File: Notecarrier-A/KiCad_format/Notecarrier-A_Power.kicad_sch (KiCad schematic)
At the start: 42 parts, among them J10 00711, J12 B2B-PH-SM4-TBT(LF)(SN), J19 MICROUSB-B, J2 B2B-PH-SM4-TBT(LF)(SN), J4 B2B-PH-SM4-TBT(LF)(SN), J9 12734, SW1 CJS-1200TA, U2 BQ24210DQCT, U3 MAX17225ELT, U4 TPS62748YFPT

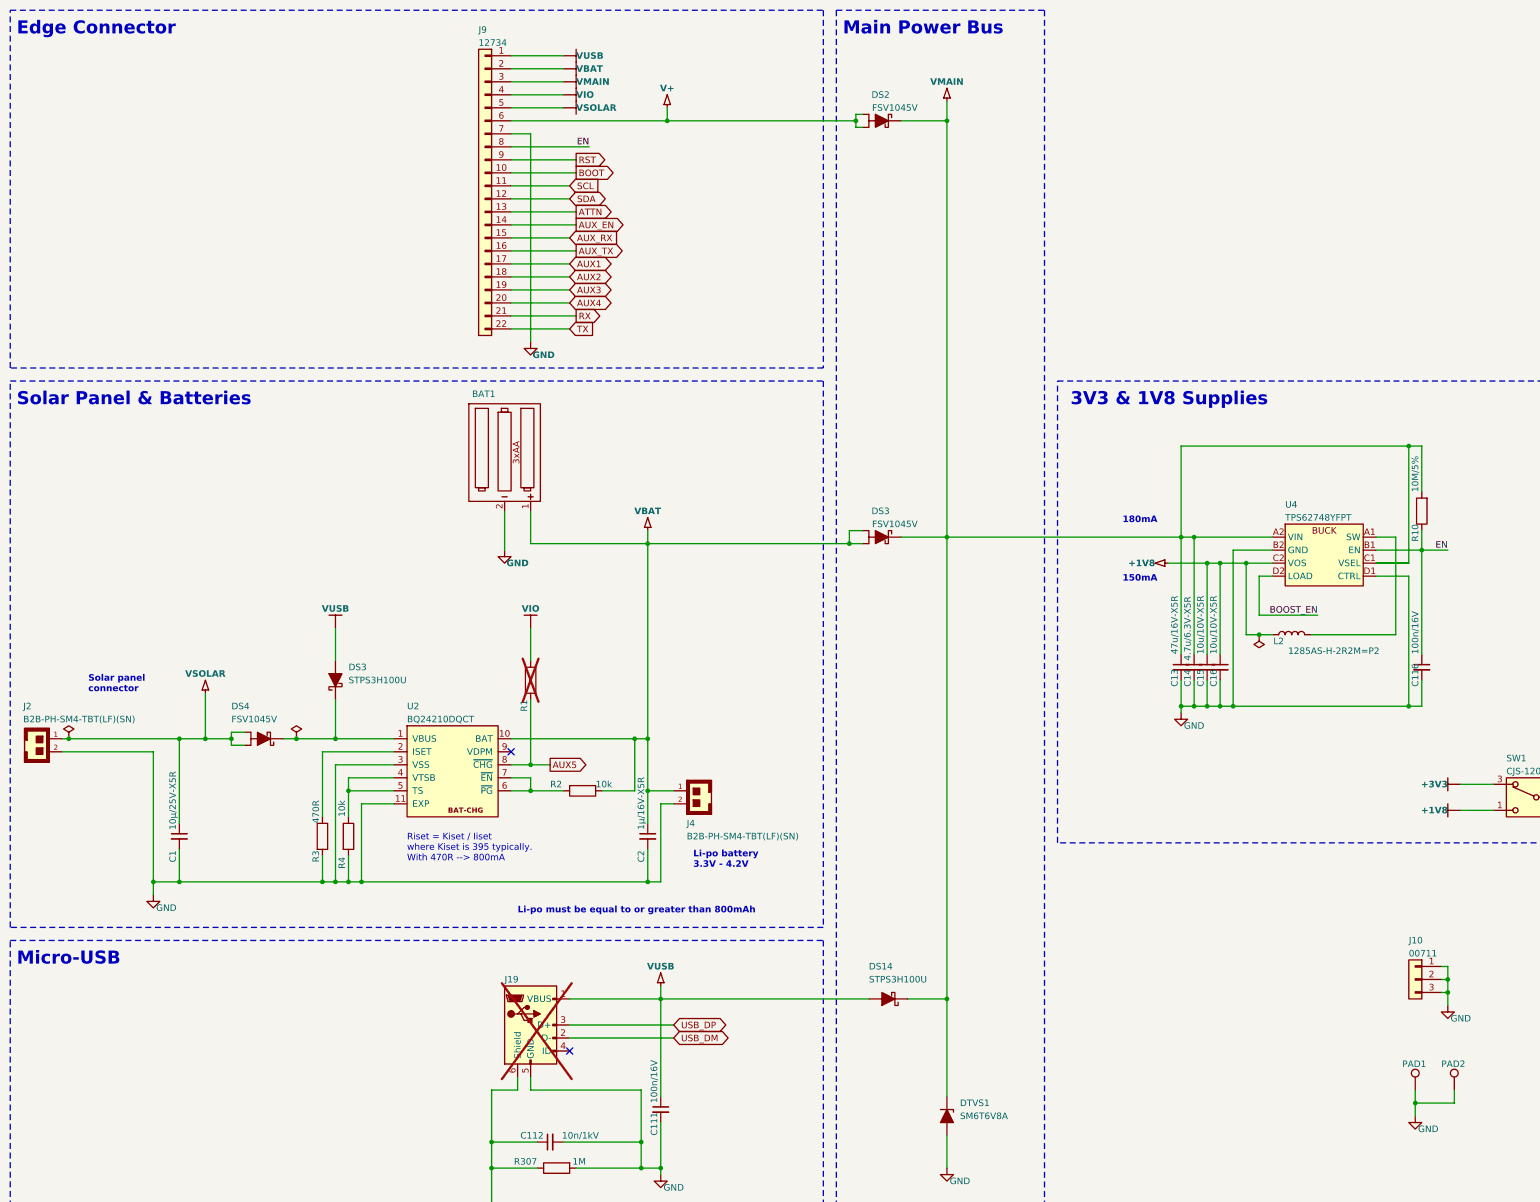
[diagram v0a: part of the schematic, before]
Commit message: Establish port of Notecarrier-B PCB.
Ported: components, board outline, fabrication layers, silkscreens and front copper.
To go: inner and back copper layers, drills, sheet metadata.
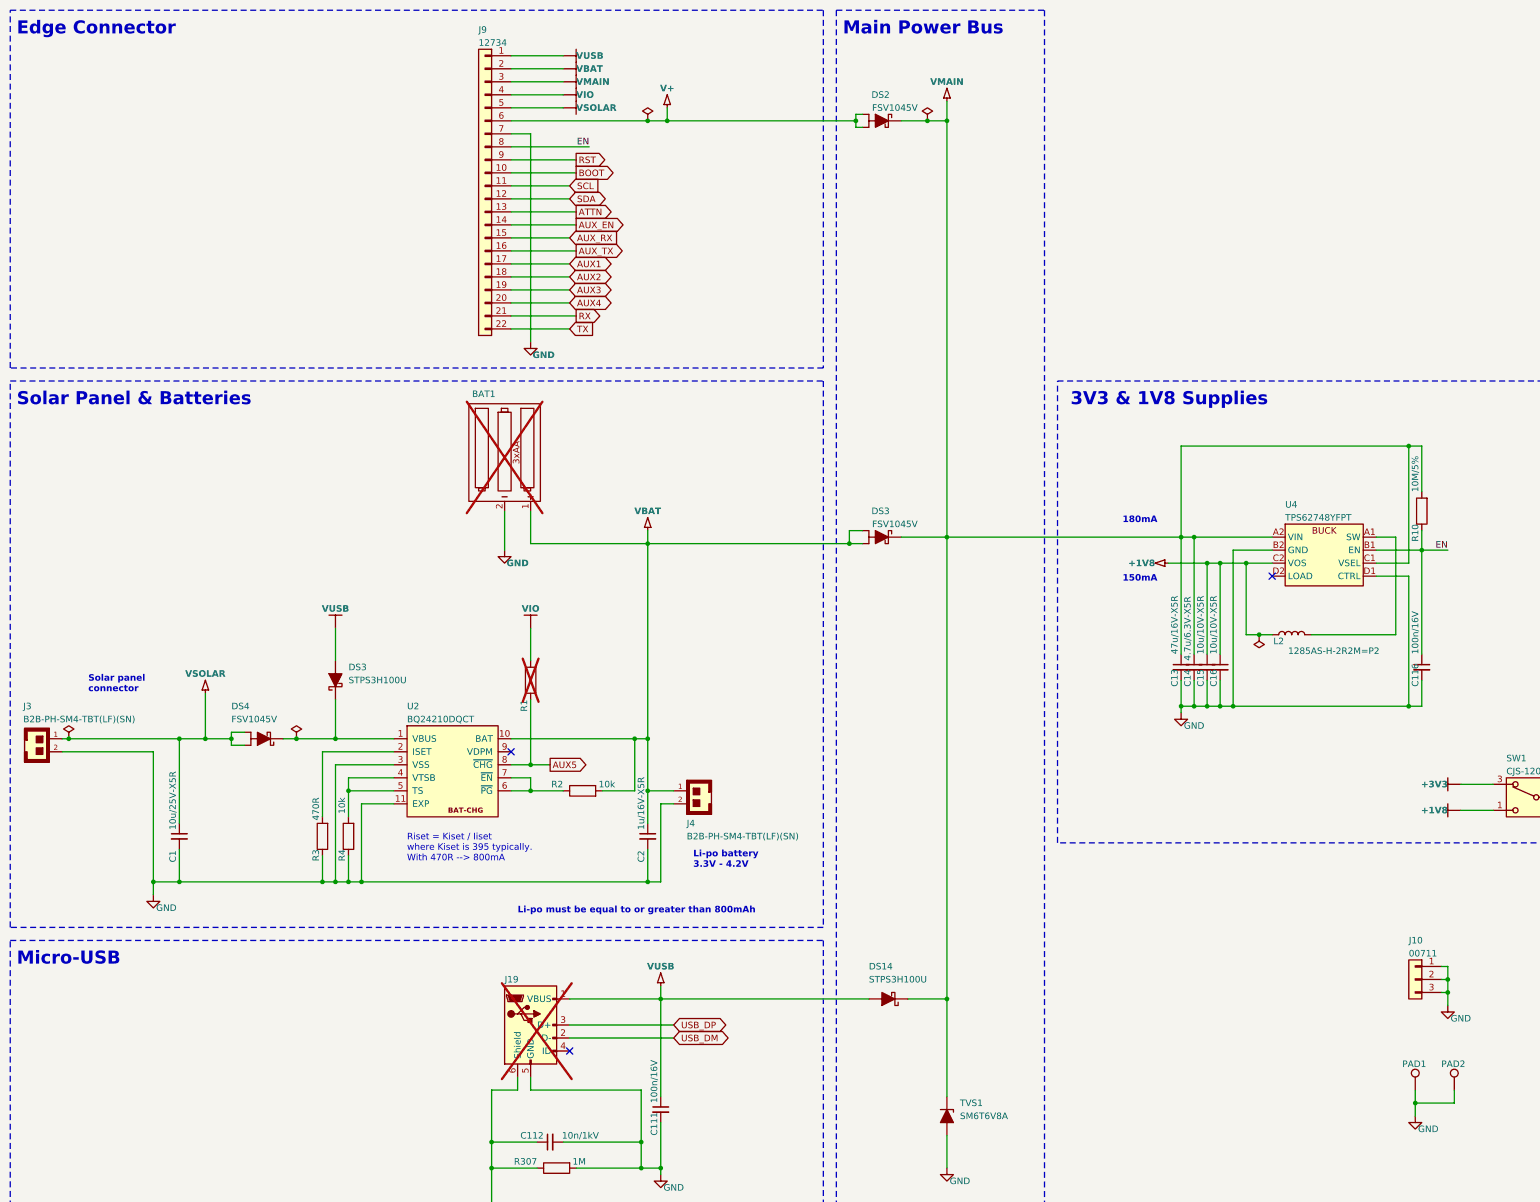
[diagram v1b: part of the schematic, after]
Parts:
- BAT1: value 3xAA -> NU; footprint (none) -> blues-kicad-lib:BATHLD-2464-NO_MECH; Caratteristiche (none) -> 3xAA; Distributor (none) -> FAE; MPN (none) -> 2464; Pkg Type (none) -> THT; now not fitted
- C1: value 10µ/25V-X5R -> 10u/25V-X5R; footprint blues-kicad-lib:CAP 1206_3216 - 0.8MM -> blues-kicad-lib:CS-C-1206; Caratteristiche (none) -> X5R; Distributor (none) -> FAE; Manufacturer Sams -> (none); Order Code 1276-1075-1-ND -> (none); Part Number CL31A106KAHNNNE -> (none); Pkg Type (none) -> SMD; Supplier Digi-Key -> (none)
- C10, C111, C112, C116, C7: Caratteristiche (none) -> X7R; Distributor (none) -> FAE
- C13, C14, C15, C16, C8, C9: Caratteristiche (none) -> X5R; Distributor (none) -> FAE
- C2: value 1µ/16V-X5R -> 1u/16V-X5R; footprint blues-kicad-lib:CAP 0402_1005 -> blues-kicad-lib:CS-C-0402; Caratteristiche (none) -> X5R; Distributor (none) -> FAE; Manufacturer Samsung -> (none); Order Code 1276-1067-1-ND -> (none); Part Number CL05A105KO5NNNC -> (none); Pkg Type (none) -> SMD; Supplier Digi-Key -> (none)
- DS14: Caratteristiche (none) -> 3A/100V; Distributor (none) -> FAE
- DS2, DS3: Caratteristiche (none) -> 10A/45V; Distributor (none) -> FAE; MPN (none) -> FSV1045V; Pkg Type (none) -> SMD; Temperature (none) -> -55°..+150°
- DS3: footprint blues-kicad-lib:DO214AA SMB -> blues-kicad-lib:SMB; symbol blues-kicad-lib:D_Schottky_Filled_Swapped -> Device:D_Schottky_Filled; Caratteristiche (none) -> 3A/100V; Distributor (none) -> FAE; MPN (none) -> STPS3H100U; Manufacturer STMicroelectronics -> (none); Order Code 497-10392-1-ND -> (none); Part Number STPS3H100U -> (none); Pkg Type (none) -> SMD; Supplier Digi-Key -> (none)
- DS4: Caratteristiche (none) -> 10A/45V; Distributor (none) -> FAE; MPN (none) -> FSV1045V; Manufacturer ON Semiconductor / Fairchild -> (none); Order Code FSV1045VCT-ND -> (none); Part Number FSV1045V -> (none); Pkg Type (none) -> SMD; Supplier Digi-Key -> (none); Temperature (none) -> -55°..+150°
- J10: footprint (none) -> blues-kicad-lib:J-3-0254-FDT_H0508; Caratteristiche (none) -> H=5.08mm; Distributor (none) -> 4UCON; MPN (none) -> 00711; Pkg Type (none) -> THT; Temperature (none) -> -55..+105
- J12, J4: footprint (none) -> blues-kicad-lib:J-2-0200-MDS-B2B-PH-SM4; Caratteristiche (none) -> 2P; Distributor (none) -> FAE; MPN (none) -> B2B-PH-SM4-TBT(LF)(SN); Manufacturer JST -> (none); Note (none) -> 100V - 2A - AWG32 to AWG24; Pkg Type (none) -> SMD; Temperature (none) -> -25°..+85°
- J19: value MICROUSB-B -> NU; footprint blues-kicad-lib:J-5-0065-FOS-MICROUSB10118192 -> blues-kicad-lib:J-5-0065-FDS-UUSB1051330001_NO-SILK; Distributor (none) -> FAE; MPN 10118192-0001LF -> 1051330001; Note (none) -> Verticale - 1.8A/30V
- J19: value MICROUSB-B -> 10118192-0002LF; Distributor (none) -> FAE; MPN 10118192-0001LF -> 10118192-0002LF; Note (none) -> Full SMD, no FLANGE; Temperature -30°..+85° -> -30°..+80°
- J3: renamed from J2; footprint (none) -> blues-kicad-lib:J-2-0200-MDS-B2B-PH-SM4; Caratteristiche (none) -> 2P; Distributor (none) -> FAE; MPN (none) -> B2B-PH-SM4-TBT(LF)(SN); Manufacturer JST -> (none); Note (none) -> 100V - 2A - AWG32 to AWG24; Pkg Type (none) -> SMD; Temperature (none) -> -25°..+85°
- J9: footprint (none) -> blues-kicad-lib:J-22-0254-FDT-H0508_EDGE; Caratteristiche (none) -> H=5.08mm; Distributor (none) -> 4UCON; MPN (none) -> 12734; Pkg Type (none) -> THT; Temperature (none) -> -55..+105
- L2: Caratteristiche (none) -> 1.5A; Distributor (none) -> FAE
- L4: Caratteristiche (none) -> 3.1A; Distributor (none) -> FAE
- PAD1, PAD2: value TestPoint -> TPS; footprint (none) -> blues-kicad-lib:PAD-THT-CAS-0100; Distributor (none) -> FAE; Pkg Type (none) -> THT
- R1: footprint blues-kicad-lib:RES 0402_1005 -> blues-kicad-lib:RS-0402; Caratteristiche (none) -> 1%; Distributor (none) -> FAE; Manufacturer TE Connectivity Passive Product -> (none); Order Code A130367CT-ND -> (none); Part Number CRGP0402F10K -> (none); Pkg Type (none) -> SMD; Supplier DigiKey -> (none); Temperature (none) -> -55°..+125°
- R10: Caratteristiche (none) -> 5%; Distributor (none) -> FAE
- R2, R4: footprint blues-kicad-lib:RES 0402_1005 -> blues-kicad-lib:RS-0402; Caratteristiche (none) -> 1%; Distributor (none) -> FAE; Manufacturer Samsung -> (none); Order Code 1276-3431-2-ND -> (none); Part Number RC1005F103CS -> (none); Pkg Type (none) -> SMD; Supplier Digi-Key -> (none); Temperature (none) -> -55°..+125°
- R3: footprint blues-kicad-lib:RES 0402_1005 -> blues-kicad-lib:RS-0402; Caratteristiche (none) -> 1%; Distributor (none) -> FAE; Manufacturer Yageo -> (none); Order Code 311-470LRTR-ND -> (none); Part Number RC0402FR-07470RL -> (none); Pkg Type (none) -> SMD; Supplier Digi-Key -> (none)
- R307, R6: Caratteristiche (none) -> 1%; Distributor (none) -> FAE
- SW1: footprint blues-kicad-lib:CJS-1200TA -> blues-kicad-lib:SW_CJS-1200TA_NO-SILK; Caratteristiche (none) -> SPDT; Distributor (none) -> FAE; Note (none) -> SPDT - 100mA/6V; Pkg Type (none) -> SMD; Temperature (none) -> -40°..+85°
- TVS1: renamed from DTVS1; footprint blues-kicad-lib-pending:SMB_Backwards -> blues-kicad-lib:SMB; Caratteristiche (none) -> 57A/6.8V/600W; Distributor (none) -> FAE; Note (none) -> Unidirezionale; Pkg Type (none) -> SMD
- U2: footprint blues-kicad-lib:BQ24210DQCT -> blues-kicad-lib:WSON10-EXP_NO-SILK; Caratteristiche (none) -> LITIO; Distributor (none) -> FAE; MPN (none) -> BQ24210DQCT; Manufacturer Texas Instruments -> (none); Note (none) -> Vin=20V - Ichg=800mA; Order Code 296-28738-1-ND -> (none); Part Number BQ24210DQCT -> (none); Pkg Type (none) -> SMD; Supplier Digi-Key -> (none); Temperature (none) -> -40°..+85°
- U3: Caratteristiche (none) -> 500mA/ADJ; Distributor (none) -> FAE; Note (none) -> 2MHz
- U4: symbol blues-kicad-lib:TPS62748 -> blues-kicad-lib:TPS62748YFPT; Caratteristiche (none) -> 300mA/ADJ; Distributor (none) -> FAE
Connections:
- net GND: now also R3.1, R4.1; no longer R3.2, R4.2
- net VBAT: now also R2.2; no longer R2.1
- net VUSB: now also DS3.2 (A); no longer DS3.1 (A)
- net at U2.4 (VTSB), U2.5 (TS): now also R4.2; no longer R4.1
- net at DS4.3 (C), U2.1 (VBUS): now also DS3.1 (K); no longer DS3.2 (K)
- net at U2.2 (ISET): now also R3.2; no longer R3.1
- net at U2.6 (~{PG}), U2.7 (~{EN}): now also R2.1; no longer R2.2
- net BOOST_EN: no longer names the net of U4.D2 (LOAD)
- no-connect marks 3 -> 4
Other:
- moved on the sheet: R2, R3, R4
